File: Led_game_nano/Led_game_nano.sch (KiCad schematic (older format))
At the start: 36 parts

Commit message: Examples of functions
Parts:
- gave numbers to parts that had none: 36
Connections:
- net LED_sig: no longer R1.2
- net at A1.22 (A3): now also R15.2
- net at A1.26 (A7): no longer R15.2
- new net DATA_PIN: R1.2
- no-connect marks 10 -> 11
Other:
- note added: "Only for analog in use"
- moved on the sheet: R15

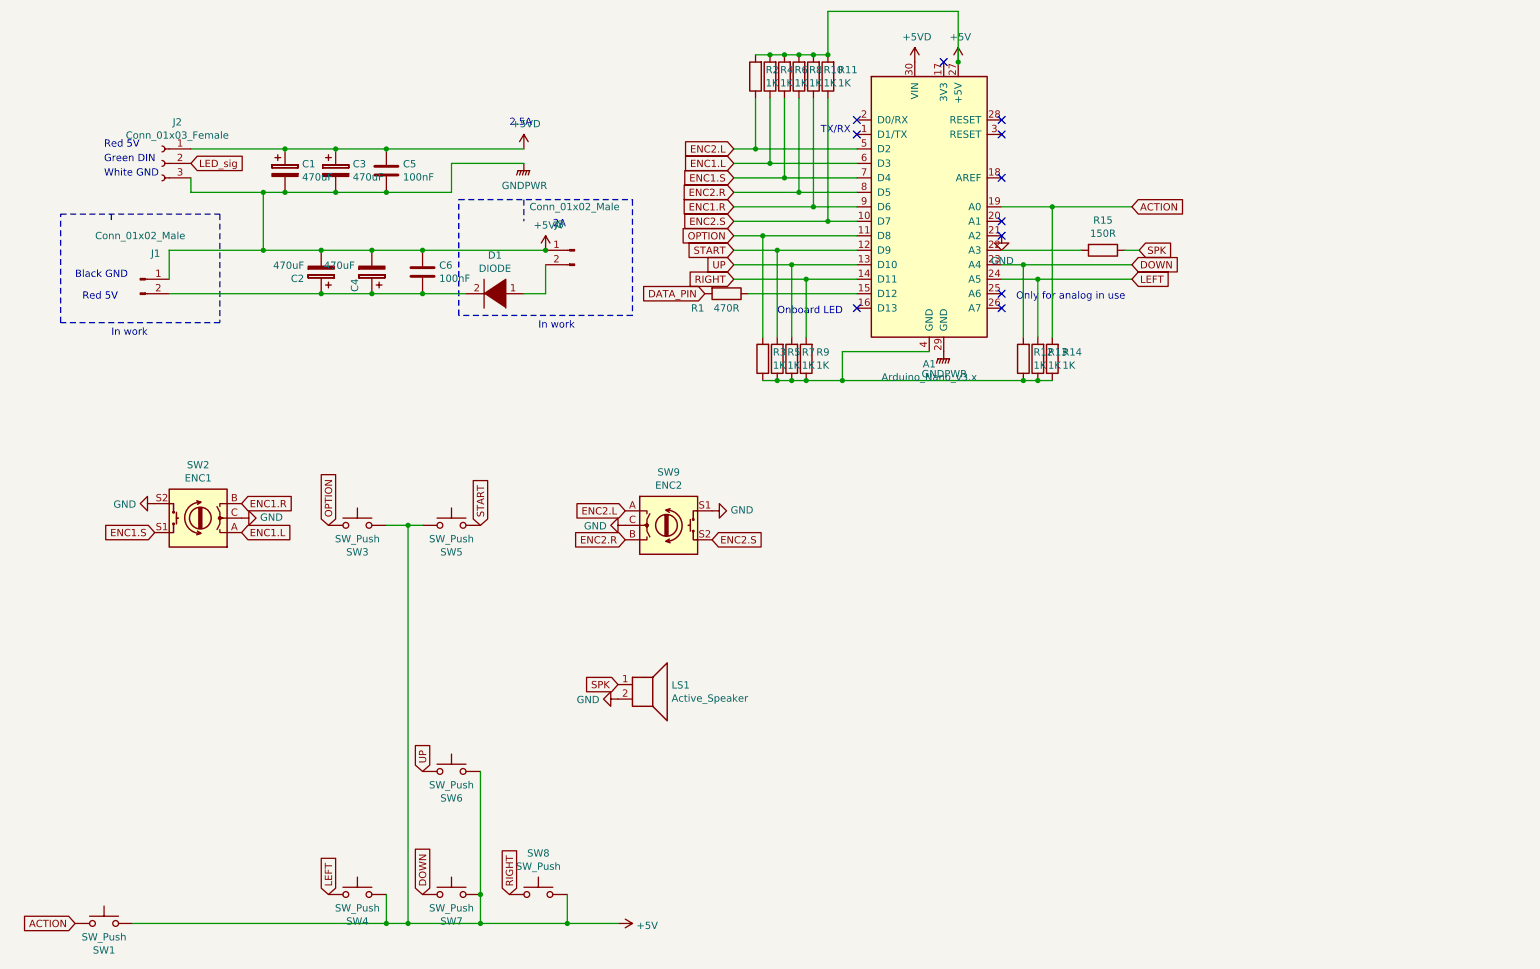
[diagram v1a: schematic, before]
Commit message: Added new power connectors to schematic
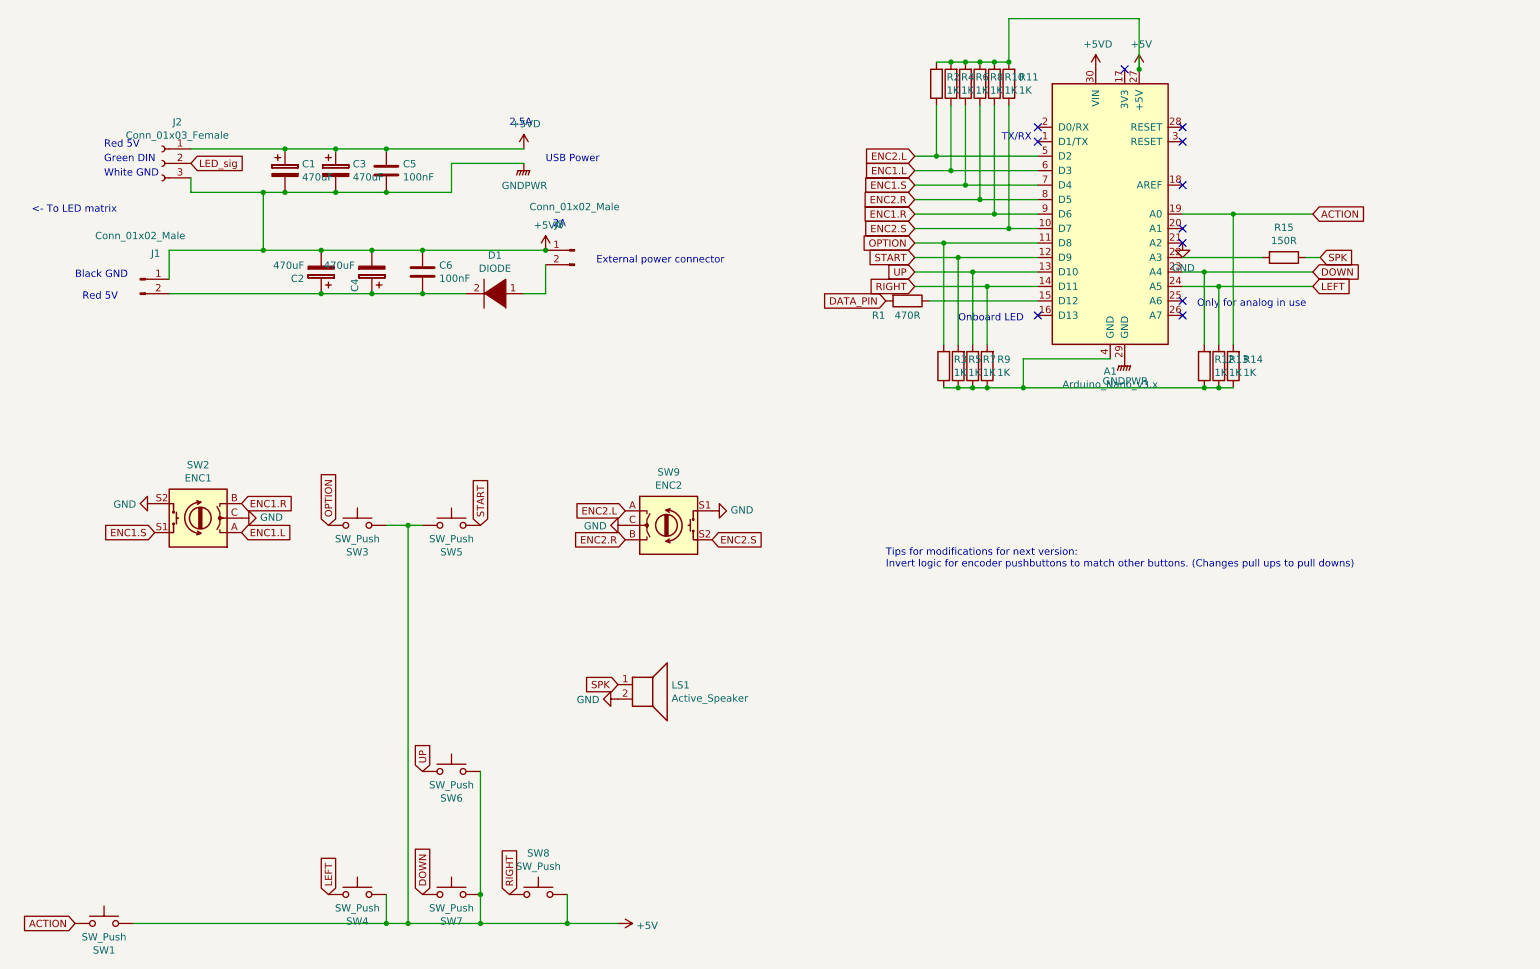
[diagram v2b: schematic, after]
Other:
- note added: "<- To LED matrix"
- note added: "External power connector"
- note added: "Tips for modifications for next version:\nInvert logic for encoder pushbuttons to match other buttons. (Changes pull ups to pull downs)"
- note added: "USB Power"
- note removed: "In work"
- moved on the sheet: A1, R1, R10, R11, R12, R13, R14, R15, R2, R3, R4, R5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
